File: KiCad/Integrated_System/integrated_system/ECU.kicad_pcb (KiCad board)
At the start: 2 copper layers, 61.3 x 72.8 mm, 57 parts, among them J1 Jack-DC, J2 Fan 1, J3 Fan 2, J4 Fan 3, J5 Conn_01x04, Q1 BSS138, Q2 BSS138, Q3 BSS138, SW1 SW_SPDT, SW2 SW_SPDT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

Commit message: add
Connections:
- SW3 pad 1: GND -> Net-(A1-IO36/A4)
- SW3 pad 2: Net-(A1-IO36/A4) -> GND
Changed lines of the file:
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@@
 			(layers "*.Cu" "*.Mask")
 			(remove_unused_layers no)
-			(net 18 "GND")
+			(net 23 "Net-(A1-IO36{slash}A4)")
 			(pinfunction "1")
 			(pintype "passive")
@@
 			(layers "*.Cu" "*.Mask")
 			(remove_unused_layers no)
-			(net 18 "GND")
+			(net 23 "Net-(A1-IO36{slash}A4)")
 			(pinfunction "1")
 			(pintype "passive")
@@
 			(layers "*.Cu" "*.Mask")
 			(remove_unused_layers no)
-			(net 23 "Net-(A1-IO36{slash}A4)")
+			(net 18 "GND")
 			(pinfunction "2")
 			(pintype "passive")
@@
 			(layers "*.Cu" "*.Mask")
 			(remove_unused_layers no)
-			(net 23 "Net-(A1-IO36{slash}A4)")
+			(net 18 "GND")
 			(pinfunction "2")
 			(pintype "passive")

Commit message: headers
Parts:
- removed J5: Conn_01x04, Connector_PinSocket_2.54mm:PinSocket_1x04_P2.54mm_Vertical
- added J6: Conn_02x04_Counter_Clockwise, Connector_PinSocket_2.54mm:PinSocket_2x04_P2.54mm_Vertical, F.Cu at (122.2, 135.0)
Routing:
- net Net-(A1-SDA/IO23): track 159.7 -> 162.5 mm
- net VDD (+ 3.3 V): track 171.4 -> 173.7 mm
- net Net-(A1-SCL/IO22): track 138.0 -> 140.1 mm
- net GND: vias 4 -> 5
- removed copper zone on B.Cu, net GND
- removed copper zone on F.Cu, net GND

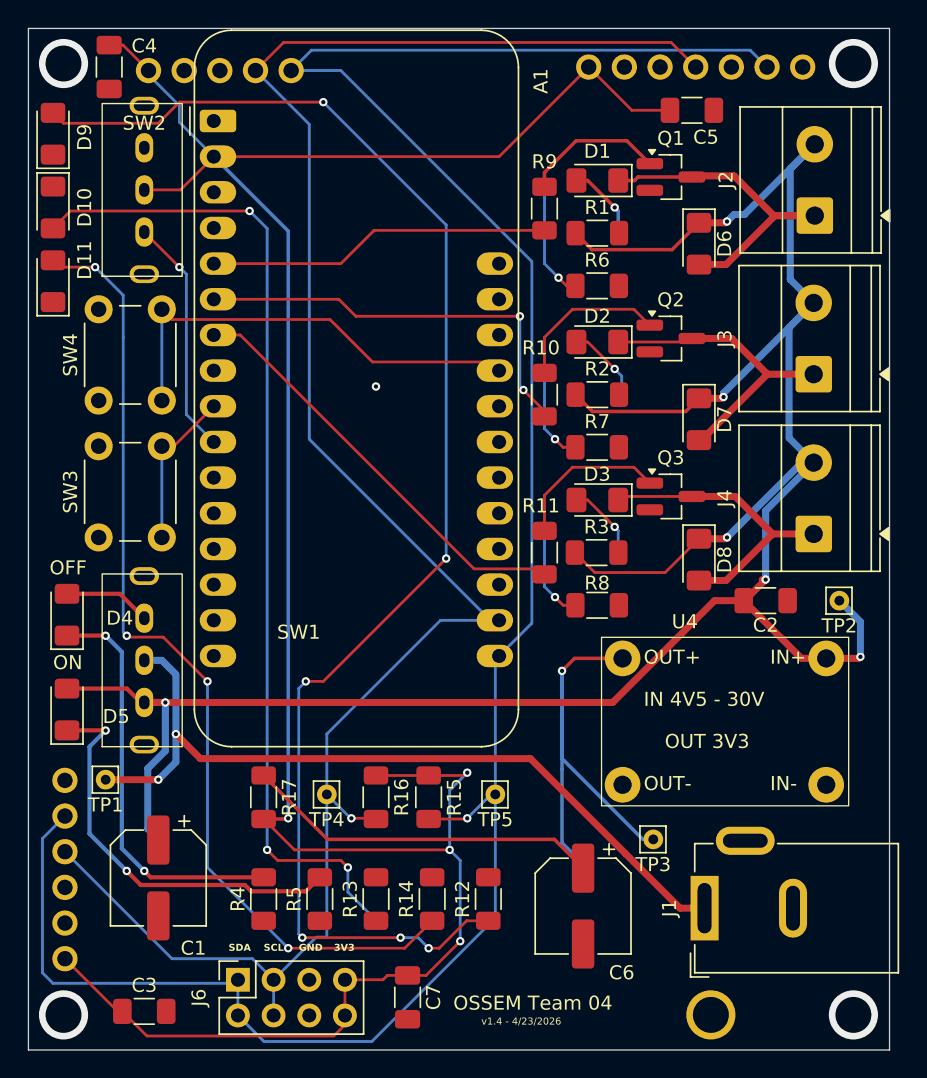
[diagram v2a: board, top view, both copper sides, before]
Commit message: added a ton of vias
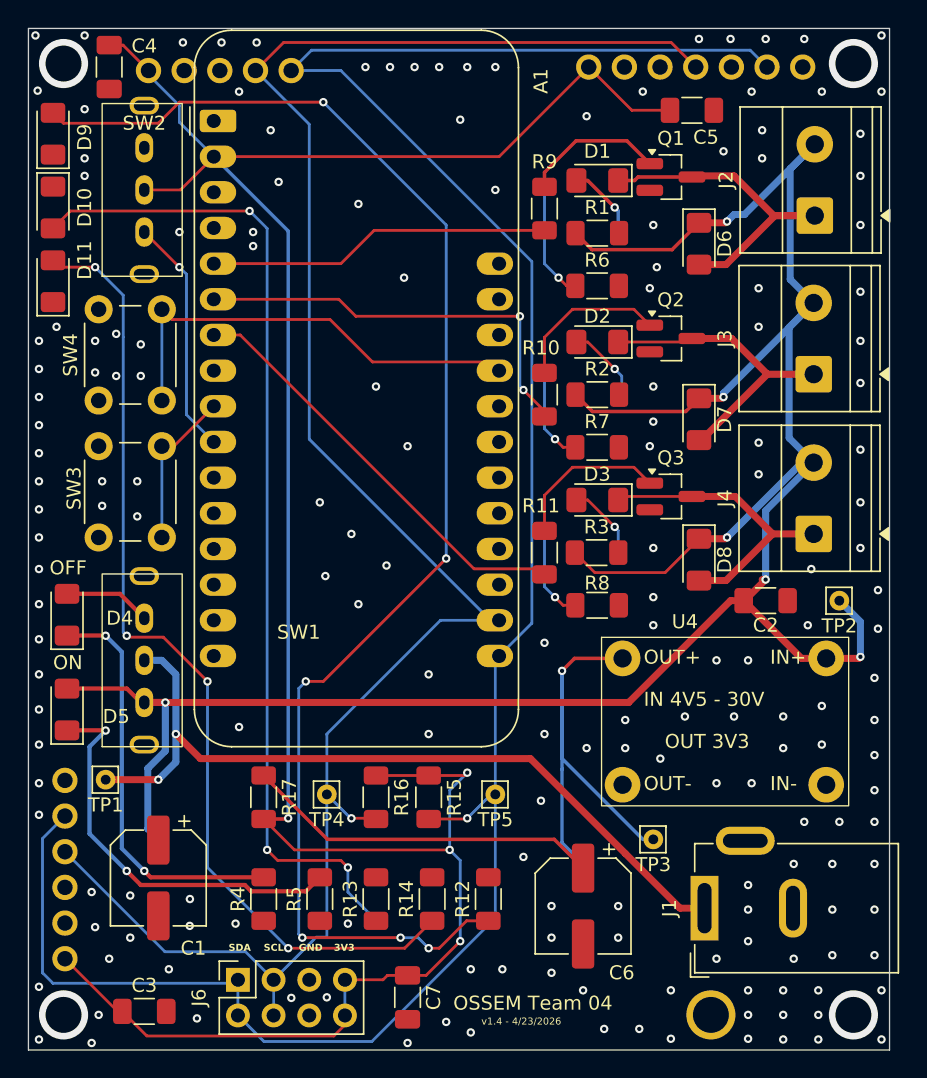
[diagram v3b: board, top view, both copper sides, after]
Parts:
- moved SW3 7.91 mm to (116.8, 97.0), turned to -90 degrees
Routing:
- net GND: vias 5 -> 185

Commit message: forgot to route some pins
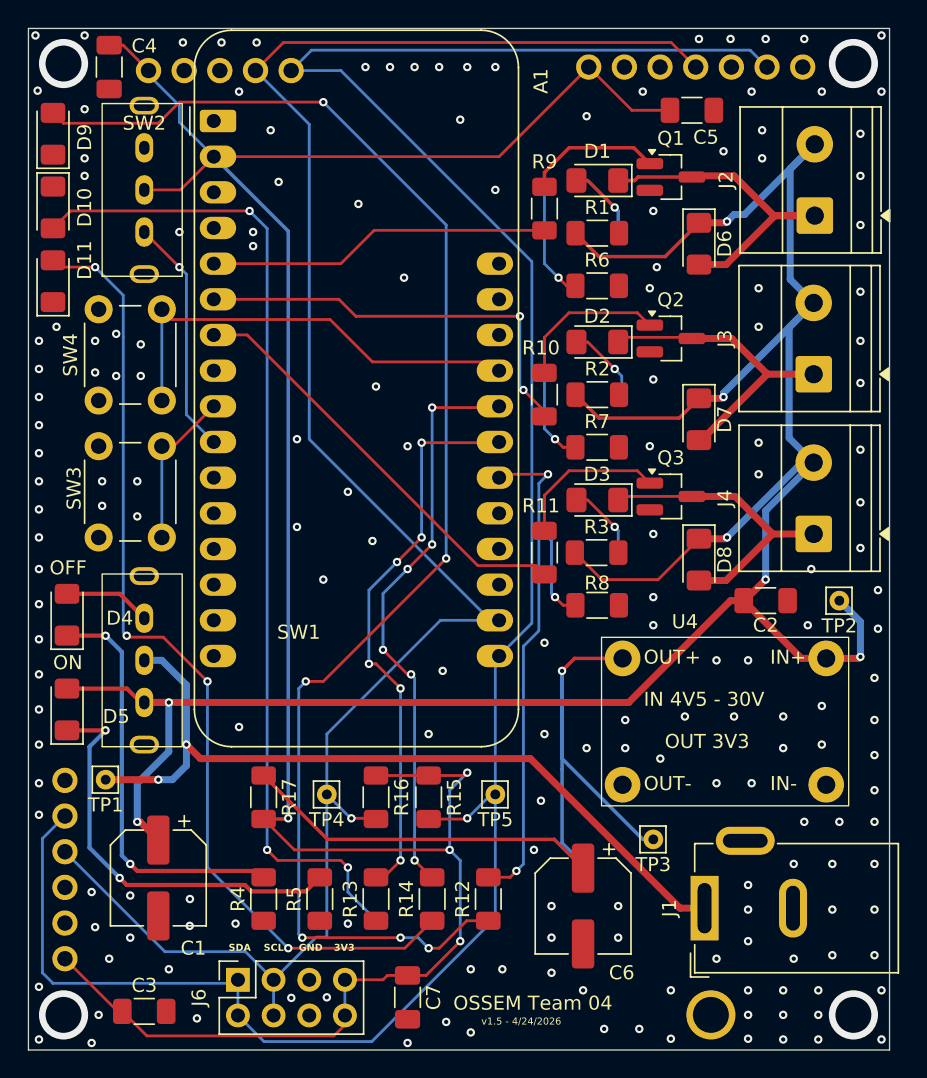
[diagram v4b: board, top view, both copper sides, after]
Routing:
- net Net-(A1-A11/IO12): track 0.00 -> 41.3 mm, vias 0 -> 6
- net Net-(A1-A10/IO27): track 0.00 -> 40.3 mm, vias 0 -> 6
- net Net-(A1-A9/IO33): track 0.51 -> 35.5 mm, vias 0 -> 2
- net FP_12V: track 178.7 -> 180.8 mm, vias 6 -> 7
- net Net-(D5-K): track 29.1 -> 29.7 mm
- net GND: vias 185 -> 184
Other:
- board text added: "v1.5 - 4/24/2026"
- board text removed: "v1.4 - 4/23/2026"

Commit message: Fixed DRC Errors
One left we need to figure out how to fix it
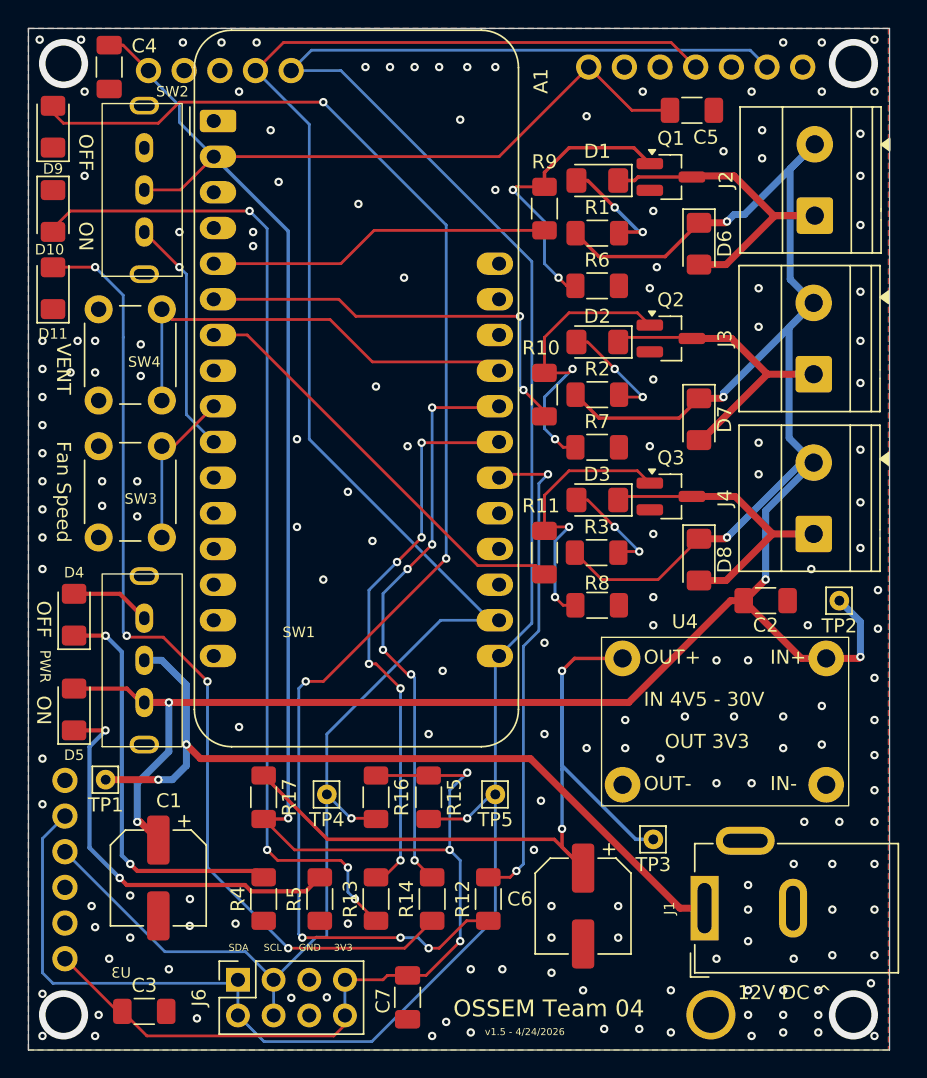
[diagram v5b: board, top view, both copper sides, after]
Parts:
- moved D11 0.50 mm to (109.0, 85.8)
- moved D4 0.50 mm to (110.5, 109.0)
- moved D5 0.50 mm to (110.5, 115.8)
- moved D9 0.50 mm to (109.0, 74.2)
- moved D10 0.25 mm to (109.0, 80.2)
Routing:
- net Net-(Q2-G): track 17.9 -> 21.1 mm, vias 1 -> 2
- net Net-(Q1-G): track 18.1 -> 21.1 mm, vias 1 -> 2
- net Net-(D1-A): track 5.12 -> 7.97 mm, vias 1 -> 2
- net Net-(D2-A): track 5.48 -> 8.11 mm, vias 1 -> 2
- net Net-(Q3-G): track 17.6 -> 20.1 mm, vias 1 -> 2
- net Net-(D3-A): track 5.37 -> 7.52 mm, vias 1 -> 2
- net Net-(U4-Vout+): track 59.7 -> 60.3 mm, vias 1 -> 2
- net Net-(D10-A): vias 3 -> 4
- net GND: vias 184 -> 174
- added copper zone on B.Cu, net GND
- added copper zone on F.Cu, net GND
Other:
- board text added: "12V DC ^"
- board text added: "Fan Speed"
- board text added: "PWR"
- board text added: "VENT"
- board text removed: "MOX Gas Sensor"
